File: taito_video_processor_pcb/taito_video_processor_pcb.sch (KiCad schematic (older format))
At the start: 237 parts, among them J1 14pin, J19 2pin, J2 14pin, J3 50pin, J6 50pin, Q1 2N3904, Q2 2N3904, Q3 2N3904, Q4 2N3904, Q5 2N3904, Q6 2N3904, Q7 2N3904, Q8 2N3905, SW1 SW_Push, U1 245_1, U10 4116, U100 LS00, U101 LS08, U102 LS10, U103 LS00, U104 157_1, U105 299_1, U106 299_1, U107 299_1, U108 299_1, U109 299_1, U11 4116, U110 299_1, U12 4116, U13 4116, U14 4116, U15 4116, U16 4116, U17 4116, U18 68A45, U19 86_2, U2 245_1, U20 86_1, U21 157_1, U22 LS32, U23 161_1, U24 LS04, U25 374_1, U26 4116, U27 4116, U28 4116, U29 4116, U3 2114, U30 4116, U31 4116, U32 4116, U33 4116, U34 LS374, U35 153_1, U36 LS74, U37 LS08, U38 74S113, U39 LS04, U4 2114, U40 7417, U41 4116, U42 4116, U43 4116, U44 4116, U45 4116, U46 4116, U47 4116, U48 4116, U49 LS32, U5 157_1, U50 86_3, U51 LS86, U52 153_1, U53 153_1, U54 153_1, U55 157_1, U56 2148_1, U57 2148_2, U58 7417, U59 4116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

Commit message: Continued layout
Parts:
- added C1, C2, C3, C4, C5, C6, C7, C8: .1uf, symbol Device:C
- J3, J6: footprint (none) -> taito_video_processor_pcb:50Pin
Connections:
- net +5V: now also C1.1, C2.1, C3.1, C4.1, C5.1, C6.1, C7.1, C8.1
- net GND: now also C1.2, C2.2, C3.2, C4.2, C5.2, C6.2, C7.2, C8.2
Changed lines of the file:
@@
 F 0 "J3" H 1400 3675 30  0000 L CNN
 F 1 "50pin" V 1425 3450 30  0000 L CNN
-F 2 "" H 1425 3425 30  0001 C CNN
+F 2 "taito_video_processor_pcb:50Pin" H 1425 3425 30  0001 C CNN
 F 3 "" H 1425 3425 30  0001 C CNN
 	1    1425 3425
@@
 F 0 "J6" H 31603 13430 30  0000 L CNN
 F 1 "50pin" H 31603 13370 30  0000 L CNN
-F 2 "" H 31525 13375 30  0001 C CNN
+F 2 "taito_video_processor_pcb:50Pin" H 31525 13375 30  0001 C CNN
 F 3 "" H 31525 13375 30  0001 C CNN
 	1    31525 13375
@@
 Wire Notes Line
 	28900 16275 28900 10600
+$Comp
+L Device:C C4
+U 1 1 61171227
+P 28525 17275
+F 0 "C4" H 28640 17321 50  0000 L CNN
+F 1 ".1uf" H 28640 17230 50  0000 L CNN
+F 2 "" H 28563 17125 50  0001 C CNN
+F 3 "~" H 28525 17275 50  0001 C CNN
+	1    28525 17275
+	1    0    0    -1
+$EndComp
+$Comp
+L Device:C C5
+U 1 1 61175975
+P 28900 17275
+F 0 "C5" H 29015 17321 50  0000 L CNN
+F 1 ".1uf" H 29015 17230 50  0000 L CNN
+F 2 "" H 28938 17125 50  0001 C CNN
+F 3 "~" H 28900 17275 50  0001 C CNN
+	1    28900 17275
+	1    0    0    -1
+$EndComp
+$Comp
+L Device:C C6
+U 1 1 61179FCE
+P 29275 17275
+F 0 "C6" H 29390 17321 50  0000 L CNN
+F 1 ".1uf" H 29390 17230 50  0000 L CNN
+F 2 "" H 29313 17125 50  0001 C CNN
+F 3 "~" H 29275 17275 50  0001 C CNN
+	1    29275 17275
+	1    0    0    -1
+$EndComp
+$Comp
+L Device:C C7
+U 1 1 6117E636
+P 29650 17275
+F 0 "C7" H 29765 17321 50  0000 L CNN
+F 1 ".1uf" H 29765 17230 50  0000 L CNN
+F 2 "" H 29688 17125 50  0001 C CNN
+F 3 "~" H 29650 17275 50  0001 C CNN
+	1    29650 17275
+	1    0    0    -1
+$EndComp
+$Comp
+L Device:C C8
+U 1 1 61182C28
+P 30025 17275
+F 0 "C8" H 30140 17321 50  0000 L CNN
+F 1 ".1uf" H 30140 17230 50  0000 L CNN
+F 2 "" H 30063 17125 50  0001 C CNN
+F 3 "~" H 30025 17275 50  0001 C CNN
+	1    30025 17275
+	1    0    0    -1
+$EndComp
+$Comp
+L Device:C C3
+U 1 1 6116CBF6
+P 28150 17275
+F 0 "C3" H 28265 17321 50  0000 L CNN
+F 1 ".1uf" H 28265 17230 50  0000 L CNN
+F 2 "" H 28188 17125 50  0001 C CNN
+F 3 "~" H 28150 17275 50  0001 C CNN
+	1    28150 17275
+	1    0    0    -1
+$EndComp
+$Comp
+L Device:C C2
+U 1 1 611685A7
+P 27775 17275
+F 0 "C2" H 27890 17321 50  0000 L CNN
+F 1 ".1uf" H 27890 17230 50  0000 L CNN
+F 2 "" H 27813 17125 50  0001 C CNN
+F 3 "~" H 27775 17275 50  0001 C CNN
+	1    27775 17275
+	1    0    0    -1
+$EndComp
+$Comp
+L Device:C C1
+U 1 1 61164136
+P 27400 17275
+F 0 "C1" H 27515 17321 50  0000 L CNN
+F 1 ".1uf" H 27515 17230 50  0000 L CNN
+F 2 "" H 27438 17125 50  0001 C CNN
+F 3 "~" H 27400 17275 50  0001 C CNN
+	1    27400 17275
+	1    0    0    -1
+$EndComp
+$Comp
+L power:+5V #PWR0350
+U 1 1 6152E23F
+P 27400 17025
+F 0 "#PWR0350" H 27400 16875 50  0001 C CNN
+F 1 "+5V" H 27415 17198 50  0000 C CNN
+F 2 "" H 27400 17025 50  0001 C CNN
+F 3 "" H 27400 17025 50  0001 C CNN
+	1    27400 17025
+	1    0    0    -1
+$EndComp
+Wire Wire Line
+	27400 17125 27400 17075
+Wire Wire Line
+	27400 17075 27775 17075
+Wire Wire Line
+	30025 17075 30025 17125
+Wire Wire Line
+	30025 17425 30025 17475
+Wire Wire Line
+	30025 17475 29650 17475
+Wire Wire Line
+	27400 17475 27400 17425
+Wire Wire Line
+	27775 17425 27775 17475
+Connection ~ 27775 17475
+Wire Wire Line
+	27775 17475 27400 17475
+Wire Wire Line
+	28150 17425 28150 17475
+Connection ~ 28150 17475
+Wire Wire Line
+	28150 17475 27775 17475
+Wire Wire Line
+	27775 17125 27775 17075
+Connection ~ 27775 17075
+Wire Wire Line
+	27775 17075 28150 17075
+Wire Wire Line
+	28150 17125 28150 17075
+Connection ~ 28150 17075
+Wire Wire Line
+	28150 17075 28525 17075
+Wire Wire Line
+	28525 17125 28525 17075
+Connection ~ 28525 17075
+Wire Wire Line
+	28525 17075 28900 17075
+Wire Wire Line
+	28900 17125 28900 17075
+Connection ~ 28900 17075
+Wire Wire Line
+	28900 17075 29275 17075
+Wire Wire Line
+	28525 17425 28525 17475
+Connection ~ 28525 17475
+Wire Wire Line
+	28525 17475 28150 17475
+Wire Wire Line
+	28900 17425 28900 17475
+Connection ~ 28900 17475
+Wire Wire Line
+	28900 17475 28525 17475
+Wire Wire Line
+	29650 17125 29650 17075
+Connection ~ 29650 17075
+Wire Wire Line
+	29650 17075 30025 17075
+Wire Wire Line
+	29275 17125 29275 17075
+Connection ~ 29275 17075
+Wire Wire Line
+	29275 17075 29650 17075
+Wire Wire Line
+	29275 17425 29275 17475
+Connection ~ 29275 17475
+Wire Wire Line
+	29275 17475 28900 17475
+Wire Wire Line
+	29650 17425 29650 17475
+Connection ~ 29650 17475
+Wire Wire Line
+	29650 17475 29275 17475
+Wire Wire Line
+	27400 17025 27400 17075
+Connection ~ 27400 17075
+$Comp
+L power:GND #PWR0351
+U 1 1 64BAC149
+P 27400 17525
+F 0 "#PWR0351" H 27400 17275 50  0001 C CNN
+F 1 "GND" H 27405 17352 50  0000 C CNN
+F 2 "" H 27400 17525 50  0001 C CNN
+F 3 "" H 27400 17525 50  0001 C CNN
+	1    27400 17525
+	1    0    0    -1
+$EndComp
+Wire Wire Line
+	27400 17525 27400 17475
+Connection ~ 27400 17475
 $EndSCHEMATC

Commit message: Placed components
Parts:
- added C10, C11, C12, C13, C15, C16, C17, C18, C19, C20, C21, C23, C24, C25, C26, C27, C28, C29, C30, C32, C33, C34, C35, C36, C37, C38, C39, C40, C41, C43, C46, C47, C48, C49, C50, C51, C52, C53, C54, C55, C56, C57, C58, C59, C60, C62, C64, C66, C67, C68, C69, C70, C71, C72, C73, C74, C75, C76, C78, C79, C81, C82, C87: .1uf, taito_video_processor_pcb:GenericComp, symbol Device:C
- added R11, R12, R22, R23, R24, R25, R26, R27, R9: ?, taito_video_processor_pcb:GenericComp, symbol Device:R_US
- C1, C14, C2, C3, C31, C4, C5, C6, C65, C7, C8, R1, R10, R13, R14, R15, R16, R17, R18, R19, R2, R20, R21, R28, R29, R3, R30, R31, R32, R33, R34, R35, R36, R39, R4, R40, R41, R42, R43, R44, R5, R6, R7, R8: footprint (none) -> taito_video_processor_pcb:GenericComp
- C22, C42, C44, C45, C61, C63, C77, C80, C9: footprint (none) -> taito_video_processor_pcb:CapA
- FB1, FB2, FB3, FB4, FB5, FB6, FB7: footprint (none) -> taito_video_processor_pcb:FB
- J1, J2: footprint (none) -> taito_video_processor_pcb:con_14pin
- J19: footprint (none) -> taito_video_processor_pcb:con_2pin
- Q1, Q2, Q3, Q4, Q5, Q6, Q7, Q8: footprint (none) -> taito_video_processor_pcb:Trans
- RP1, RP2, RP3, RP4, RP5: footprint (none) -> taito_video_processor_pcb:RP
- TP1, TP2, TP3, TP4: footprint (none) -> taito_video_processor_pcb:TPA
- Y1: footprint (none) -> taito_video_processor_pcb:Crystal
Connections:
- net +12V: now also C16.1, C18.1, C19.1, C21.1, C36.1, C37.1, C55.1, C59.1, C72.1, C76.1, C87.1
- net +5V: now also C10.1, C11.1, C12.1, C13.1, C15.1, C17.1, C20.1, C23.1, C26.1, C27.1, C28.1, C29.1, C30.1, C32.1, C35.1, C39.1, C41.1, C50.1, C51.1, C52.1, C56.1, C60.1, C64.1, C66.1, C67.1, C68.1, C69.1, C70.1, C71.1, C75.1, C79.1, C81.1, C82.1
- net -5V: now also C33.1, C34.1, C38.1, C40.1, C43.1, C53.1, C54.1, C57.1, C58.1, C62.1, C73.1, C74.1, C78.1
- net GND: now also C10.2, C11.2, C12.2, C13.2, C15.2, C16.2, C17.2, C18.2, C19.2, C20.2, C21.2, C23.2, C24.2, C25.2, C26.2, C27.2, C28.2, C29.2, C30.2, C32.2, C33.2, C34.2, C35.2, C36.2, C37.2, C38.2, C39.2, C40.2, C41.2, C43.2, C46.2, C47.2, C48.2, C49.2, C50.2, C51.2, C52.2, C53.2, C54.2, C55.2, C56.2, C57.2, C58.2, C59.2, C60.2, C62.2, C64.2, C66.2, C67.2, C68.2, C69.2, C70.2, C71.2, C72.2, C73.2, C74.2, C75.2, C76.2, C78.2, C79.2, C81.2, C82.2, C87.2
- net M0: now also R25.1; no longer U54.7
- net M1: now also R27.1; no longer U53.9
- net M2: now also R26.1; no longer U53.7
- net M3: now also R11.1; no longer U35.9
- net M4: now also R24.1; no longer U35.7
- net M5: now also R23.1; no longer U52.9
- net M6: now also R22.1; no longer U52.7
- net _BLUE_: now also C47.1
- net _CS_: now also C25.1
- net _GREEN_: now also C48.1
- net _HS_: now also C46.1
- net _RED_: now also C49.1
- net _VS_: now also C24.1
- net ~CAS: now also R9.2; no longer RP1.2
- net ~EVEN1: now also U67.5; no longer U67.2
- net ~ODD1: now also U67.2; no longer U67.5
- net ~RAS: now also R12.1; no longer U37.8
- net at Q1.1 (E), Q2.3 (C), Q3.3 (C)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: now also Q4.3 (C), Q5.3 (C), Q6.3 (C), Q7.3 (C), R31.1, R32.1, R33.1, R47.1
- net at U67.6: now also R36.2; no longer R21.2
- net at U67.3: now also R21.2; no longer R36.2
- net MUX: no longer names the net of U36.11 (2CLK), U38.9 (Q)
- new net: R22.2, U52.7
- new net: R23.2, U52.9
- new net: R24.2, U35.7
- new net: R11.2, U35.9
- new net: R26.2, U53.7
- new net: R27.2, U53.9
- new net: R25.2, U54.7
- new net: R12.2, U37.8
- new net ~CAS1: R9.1, RP1.2
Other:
- moved on the sheet: C1, C2, C3, C4, C5, C6, C7, C8, U35, U52, U53, U54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

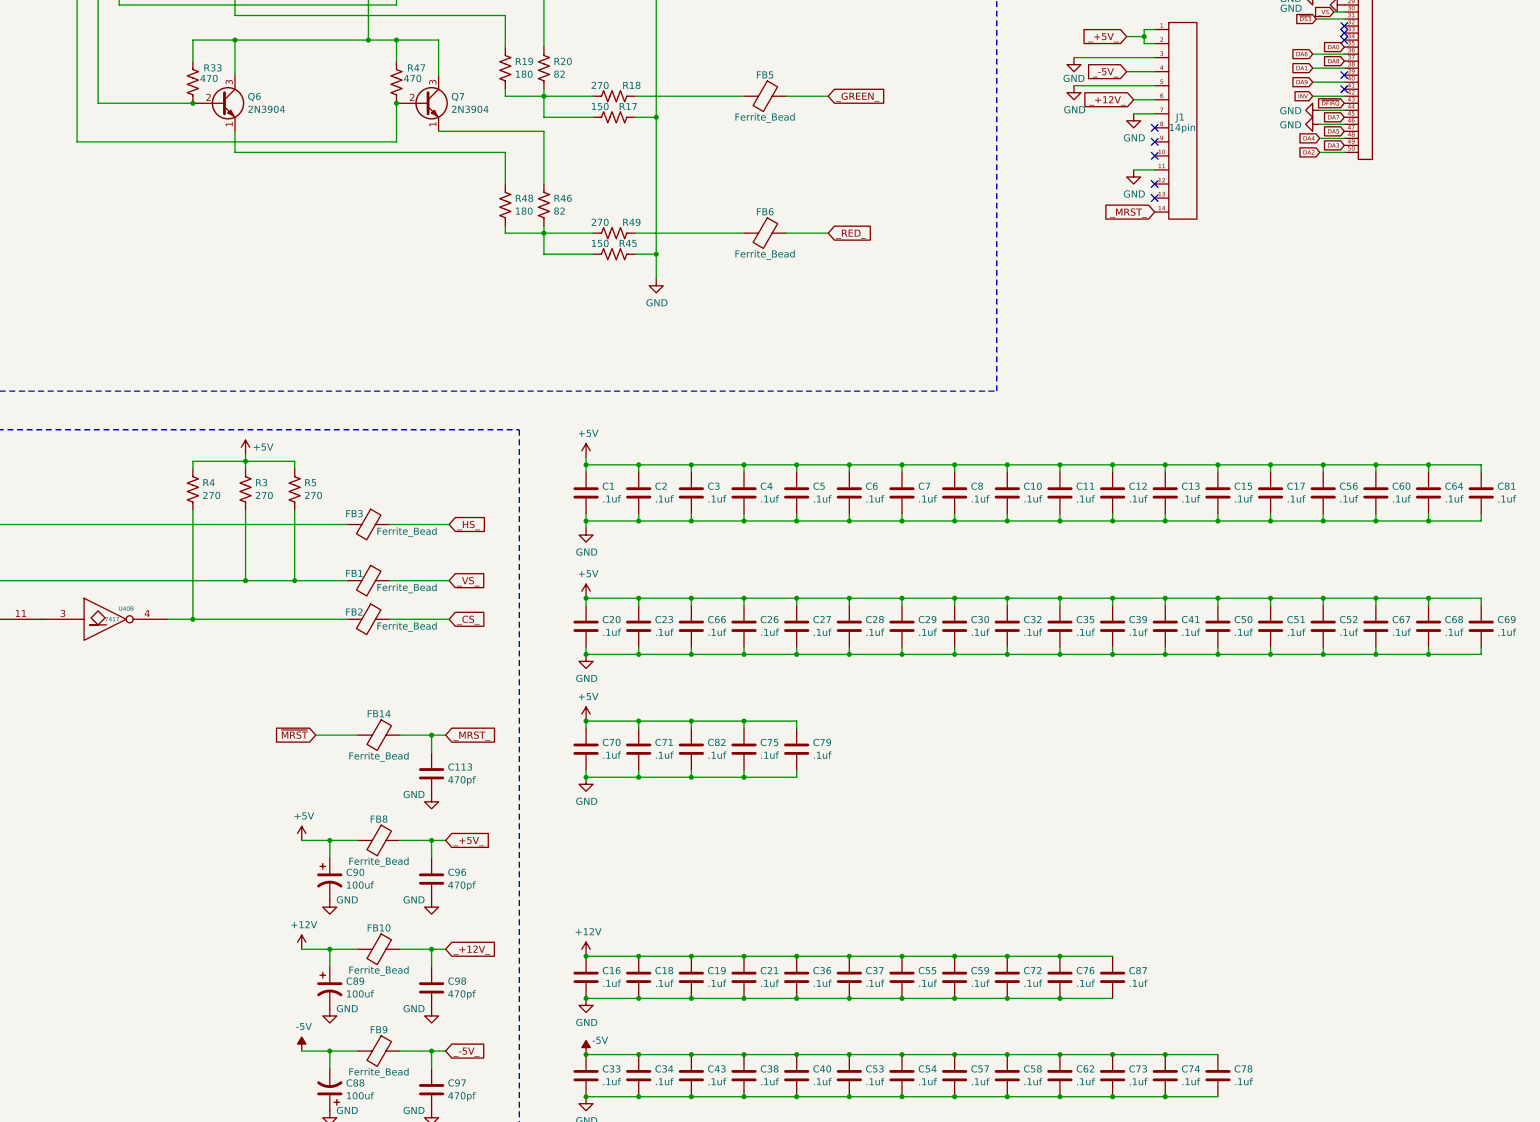
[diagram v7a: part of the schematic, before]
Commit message: Finished placing components
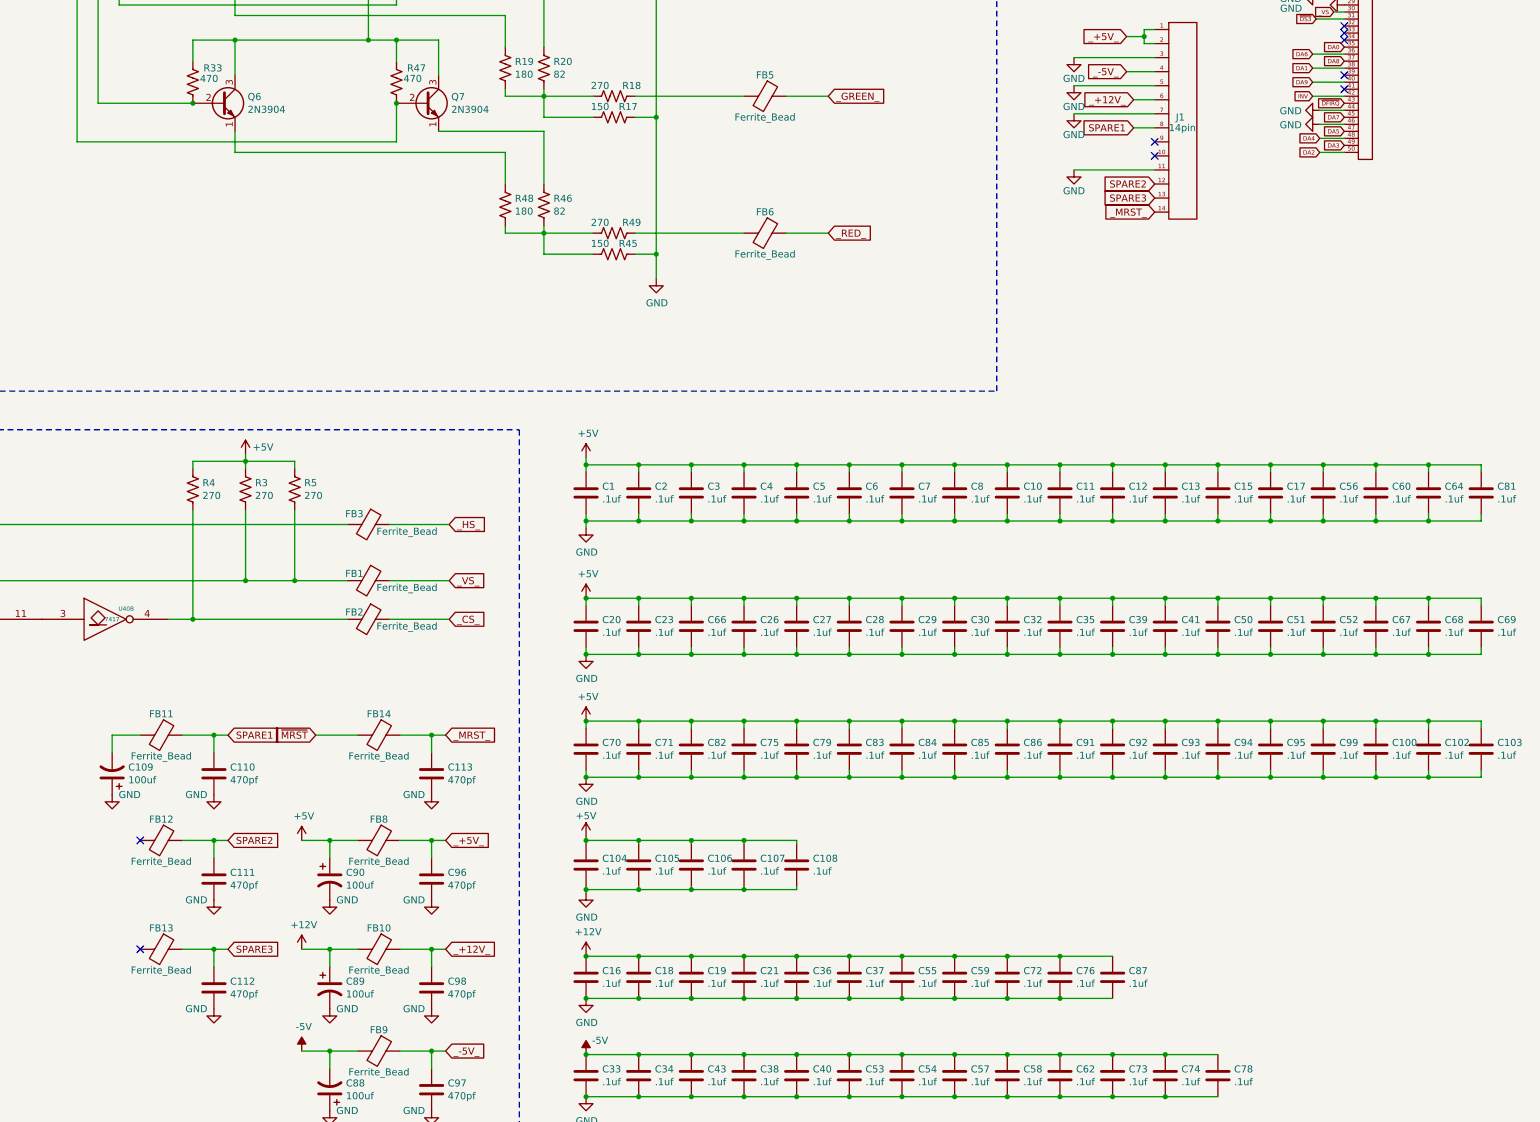
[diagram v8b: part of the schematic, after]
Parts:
- added C100, C102, C103, C104, C105, C106, C107, C108, C83, C84, C85, C86, C91, C92, C93, C94, C95, C99: .1uf, taito_video_processor_pcb:GenericComp, symbol Device:C
- added C109: 100uf, taito_video_processor_pcb:CapB, symbol Device:CP1
- added C110, C111, C112: 470pf, taito_video_processor_pcb:GenericComp, symbol Device:C
- added FB11, FB12, FB13: Ferrite_Bead, taito_video_processor_pcb:FB, symbol Device:Ferrite_Bead
- BT1: footprint (none) -> taito_video_processor_pcb:battery
- C101, C113, C96, C97, C98, R37, R38, R45, R46, R47, R48, R49, R50, R51, R52, R53, R54, R55, R56, R57, R58, R59, R60, R61, R62, R63, R64, R65, R66, R67, R68, R69: footprint (none) -> taito_video_processor_pcb:GenericComp
- C88, C89, C90: footprint (none) -> taito_video_processor_pcb:CapB
- FB10, FB14, FB8, FB9: footprint (none) -> taito_video_processor_pcb:FB
- JB2: footprint (none) -> taito_video_processor_pcb:JMP
- LED1, LED2, LED3, LED4, LED5, LED6: footprint (none) -> taito_video_processor_pcb:LED
- SW1: footprint (none) -> taito_video_processor_pcb:Switch
- TP5, TP6, TP7, TP8: footprint (none) -> taito_video_processor_pcb:TPB
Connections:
- net +5V: now also C100.1, C102.1, C103.1, C104.1, C105.1, C106.1, C107.1, C108.1, C83.1, C84.1, C85.1, C86.1, C91.1, C92.1, C93.1, C94.1, C95.1, C99.1
- net GND: now also C100.2, C102.2, C103.2, C104.2, C105.2, C106.2, C107.2, C108.2, C109.1, C110.2, C111.2, C112.2, C83.2, C84.2, C85.2, C86.2, C91.2, C92.2, C93.2, C94.2, C95.2, C99.2
- net SPARE2: now reaches J1.12
- net SPARE2: now also C111.1, FB12.1
- net SPARE3: now reaches J1.13
- net SPARE3: now also C112.1, FB13.1
- net SPARE1: now reaches J1.8
- net SPARE1: now also C110.1, FB11.1
- new net: C109.2, FB11.2
- no-connect marks 93 -> 92
